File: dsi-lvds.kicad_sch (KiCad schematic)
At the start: 27 parts, among them Q1 PJE138K, U1 TLV70018_SC70, U2 TXB0104_UQFN, U3 SN65DSI84

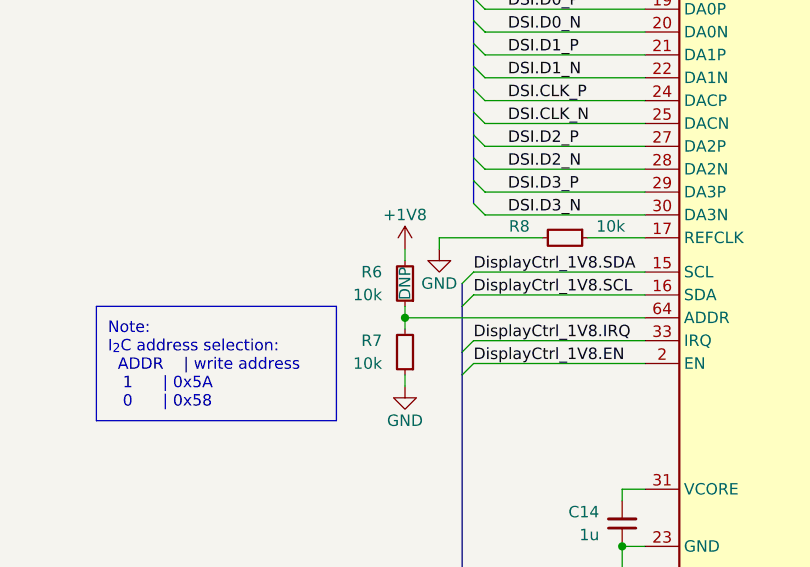
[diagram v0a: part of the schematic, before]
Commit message: [#54932] PCB: move all components inside board outline; Sch: clean DNP's
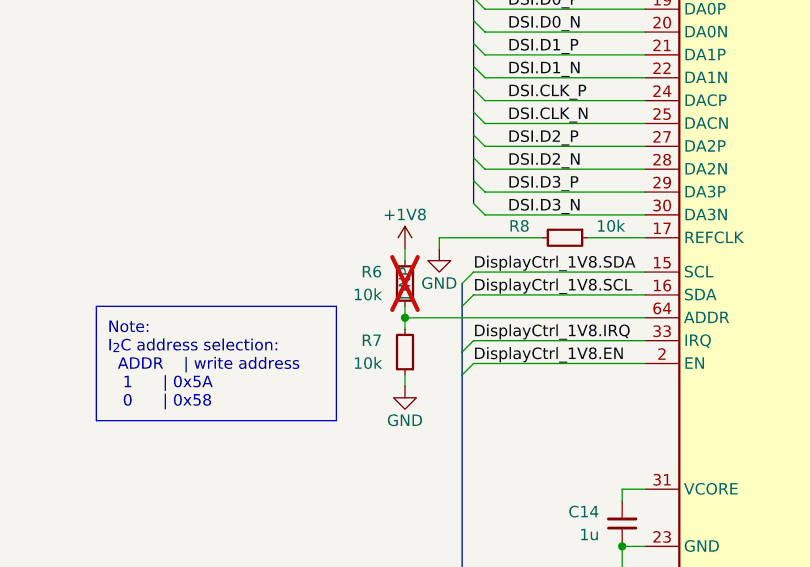
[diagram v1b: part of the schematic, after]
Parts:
- R6: now not fitted; now left out of the parts list
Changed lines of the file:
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@@
   )
   (symbol (lib_id "antmicroResistors0402:R_10k_0402") (at 219.71 135.89 270) (mirror x) (unit 1)
-    (in_bom yes) (on_board yes) (dnp no)
+    (in_bom no) (on_board yes) (dnp yes)
     (property "Reference" "R6" (at 217.17 132.0799 90)
       (effects (font (size 1.27 1.27) (thickness 0.15)) (justify right))

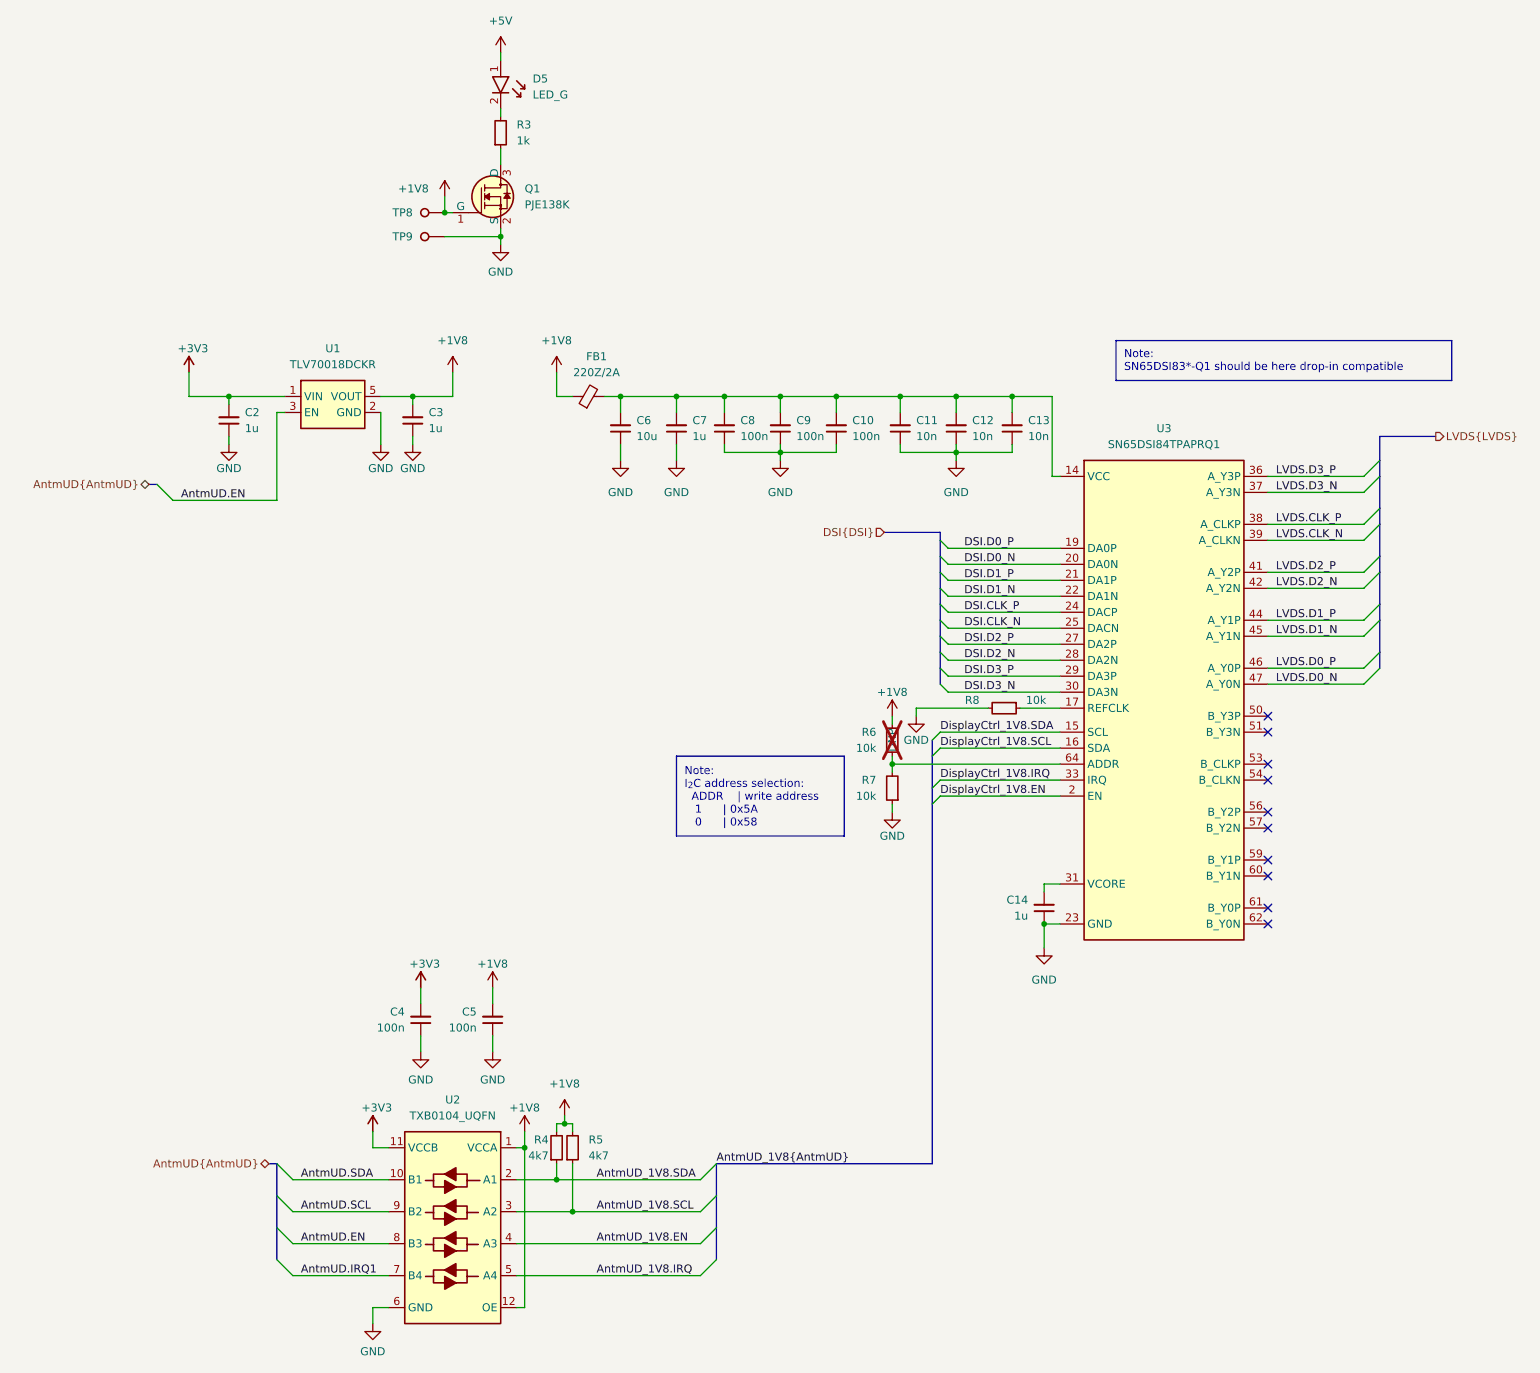
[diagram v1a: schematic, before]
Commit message: [#54932] Sch: update net labels
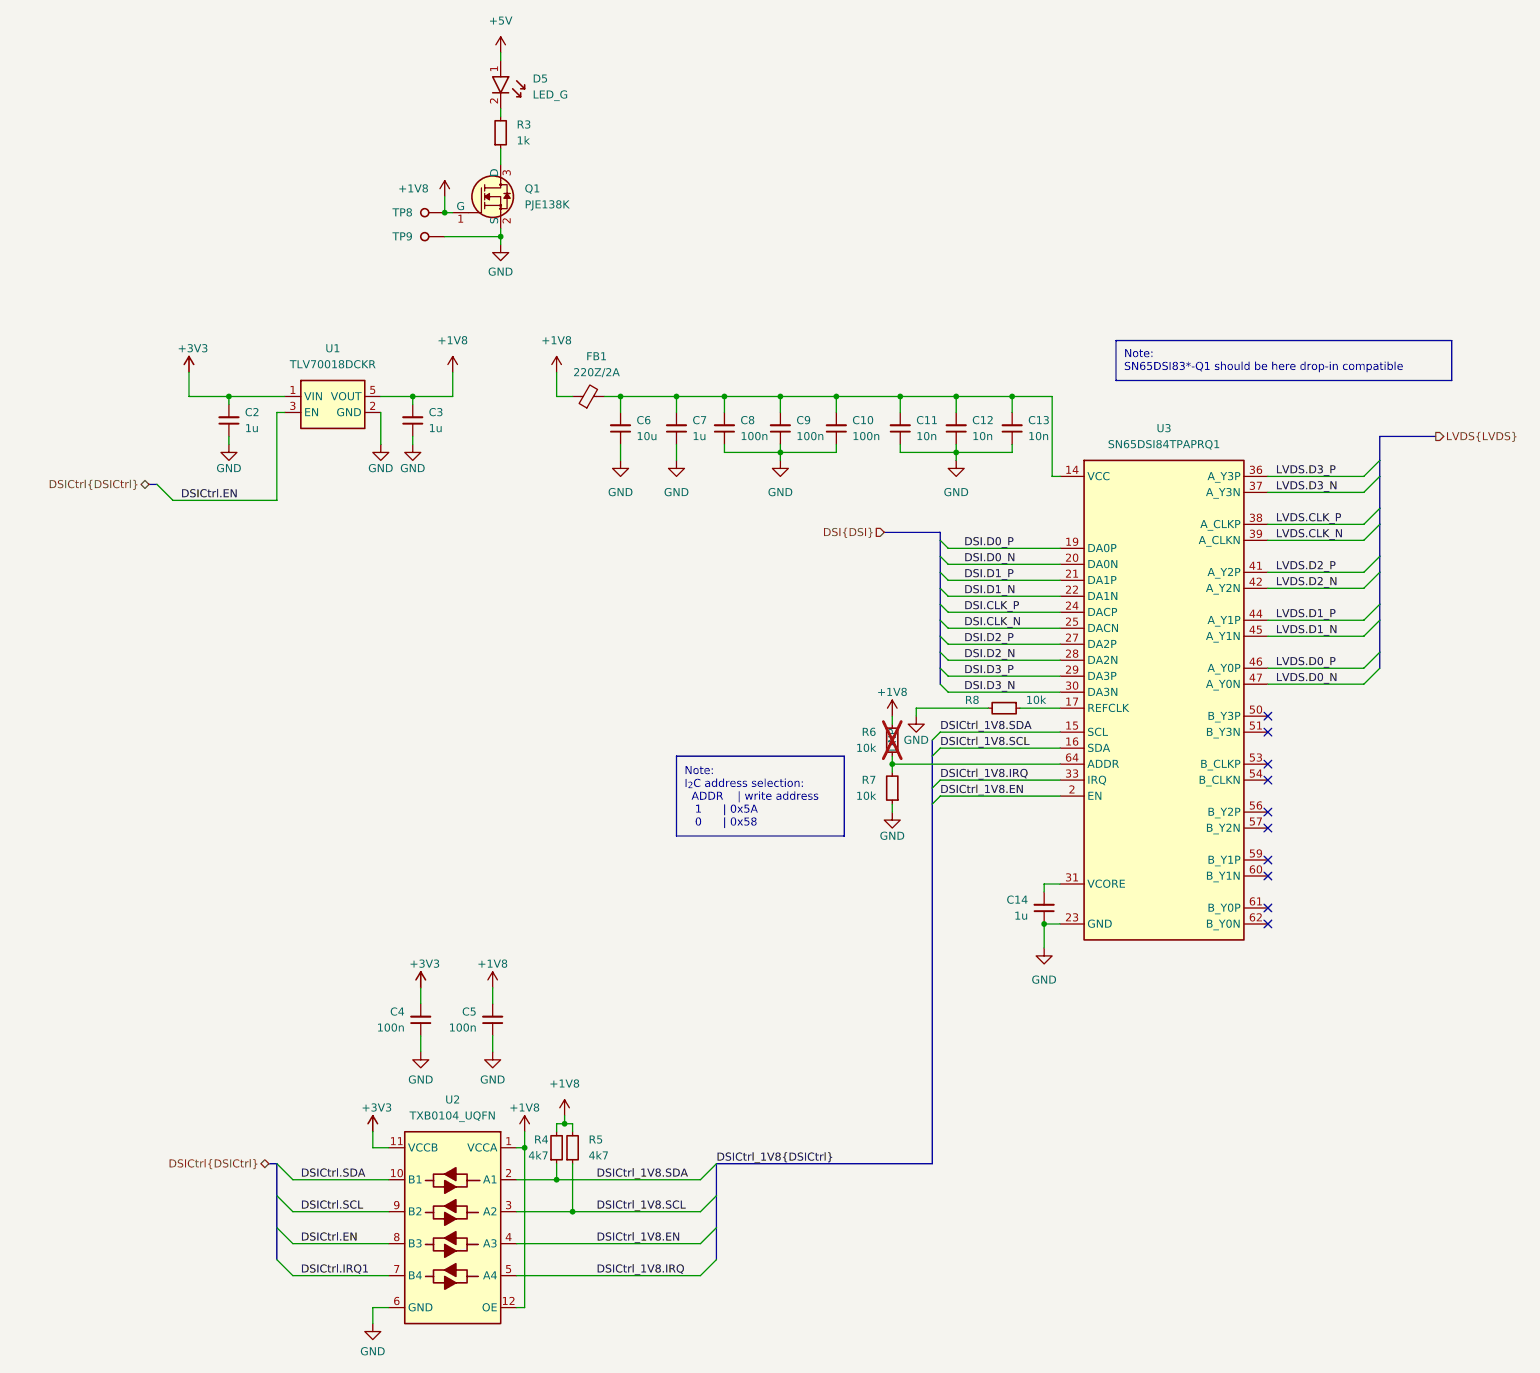
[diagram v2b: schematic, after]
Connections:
- net DisplayCtrl_1V8.EN is gone; now on net DSICtrl_1V8.EN: U3.2 (EN)
- net DisplayCtrl_1V8.IRQ is gone; now on net DSICtrl_1V8.IRQ: U3.33 (IRQ)
- net DisplayCtrl_1V8.SCL is gone; now on net DSICtrl_1V8.SCL: U3.16 (SDA)
- net DisplayCtrl_1V8.SDA is gone; now on net DSICtrl_1V8.SDA: U3.15 (SCL)
- net AntmUD.EN renamed DSICtrl.EN
- net AntmUD.IRQ1 renamed DSICtrl.IRQ1
- net AntmUD.SCL renamed DSICtrl.SCL
- net AntmUD.SDA renamed DSICtrl.SDA
- net AntmUD_1V8.EN renamed DSICtrl_1V8.EN
- net AntmUD_1V8.IRQ renamed DSICtrl_1V8.IRQ
- net AntmUD_1V8.SCL renamed DSICtrl_1V8.SCL
- net AntmUD_1V8.SDA renamed DSICtrl_1V8.SDA
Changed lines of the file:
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@@
     (effects (font (size 1.27 1.27)) (justify left bottom))
   )
-  (label "AntmUD.IRQ1" (at 125.73 218.44 0) (fields_autoplaced)
+  (label "DSICtrl.IRQ1" (at 125.73 218.44 0) (fields_autoplaced)
     (effects (font (size 1.27 1.27)) (justify left bottom))
   )
@@
     (effects (font (size 1.27 1.27)) (justify left bottom))
   )
-  (label "AntmUD.EN" (at 125.73 213.36 0) (fields_autoplaced)
+  (label "DSICtrl.EN" (at 125.73 213.36 0) (fields_autoplaced)
     (effects (font (size 1.27 1.27)) (justify left bottom))
   )
@@
     (effects (font (size 1.27 1.27)) (justify left bottom))
   )
-  (label "DisplayCtrl_1V8.IRQ" (at 227.33 139.7 0) (fields_autoplaced)
+  (label "DSICtrl_1V8.IRQ" (at 227.33 139.7 0) (fields_autoplaced)
     (effects (font (size 1.27 1.27)) (justify left bottom))
   )
@@
     (effects (font (size 1.27 1.27)) (justify left bottom))
   )
-  (label "AntmUD_1V8.SDA" (at 172.72 203.2 0) (fields_autoplaced)
+  (label "DSICtrl_1V8.SDA" (at 172.72 203.2 0) (fields_autoplaced)
     (effects (font (size 1.27 1.27)) (justify left bottom))
   )
-  (label "AntmUD_1V8.IRQ" (at 172.72 218.44 0) (fields_autoplaced)
+  (label "DSICtrl_1V8.IRQ" (at 172.72 218.44 0) (fields_autoplaced)
     (effects (font (size 1.27 1.27)) (justify left bottom))
   )
@@
     (effects (font (size 1.27 1.27)) (justify left bottom))
   )
-  (label "AntmUD.EN" (at 106.68 95.25 0) (fields_autoplaced)
+  (label "DSICtrl.EN" (at 106.68 95.25 0) (fields_autoplaced)
     (effects (font (size 1.27 1.27)) (justify left bottom))
   )
@@
     (effects (font (size 1.27 1.27)) (justify left bottom))
   )
-  (label "AntmUD.SCL" (at 125.73 208.28 0) (fields_autoplaced)
+  (label "DSICtrl.SCL" (at 125.73 208.28 0) (fields_autoplaced)
     (effects (font (size 1.27 1.27)) (justify left bottom))
   )
@@
     (effects (font (size 1.27 1.27)) (justify left bottom))
   )
-  (label "DisplayCtrl_1V8.SDA" (at 227.33 132.08 0) (fields_autoplaced)
+  (label "DSICtrl_1V8.SDA" (at 227.33 132.08 0) (fields_autoplaced)
     (effects (font (size 1.27 1.27)) (justify left bottom))
   )
@@
     (effects (font (size 1.27 1.27)) (justify left bottom))
   )
-  (label "AntmUD_1V8.EN" (at 172.72 213.36 0) (fields_autoplaced)
+  (label "DSICtrl_1V8.EN" (at 172.72 213.36 0) (fields_autoplaced)
     (effects (font (size 1.27 1.27)) (justify left bottom))
   )
@@
     (effects (font (size 1.27 1.27)) (justify left bottom))
   )
-  (label "AntmUD_1V8.SCL" (at 172.72 208.28 0) (fields_autoplaced)
+  (label "DSICtrl_1V8.SCL" (at 172.72 208.28 0) (fields_autoplaced)
     (effects (font (size 1.27 1.27)) (justify left bottom))
   )
-  (label "DisplayCtrl_1V8.SCL" (at 227.33 134.62 0) (fields_autoplaced)
+  (label "DSICtrl_1V8.SCL" (at 227.33 134.62 0) (fields_autoplaced)
     (effects (font (size 1.27 1.27)) (justify left bottom))
   )
-  (label "AntmUD_1V8{AntmUD}" (at 191.77 200.66 0) (fields_autoplaced)
+  (label "DSICtrl_1V8{DSICtrl}" (at 191.77 200.66 0) (fields_autoplaced)
     (effects (font (size 1.27 1.27)) (justify left bottom))
   )
@@
     (effects (font (size 1.27 1.27)) (justify left bottom))
   )
-  (label "AntmUD.SDA" (at 125.73 203.2 0) (fields_autoplaced)
+  (label "DSICtrl.SDA" (at 125.73 203.2 0) (fields_autoplaced)
     (effects (font (size 1.27 1.27)) (justify left bottom))
   )
-  (label "DisplayCtrl_1V8.EN" (at 227.33 142.24 0) (fields_autoplaced)
+  (label "DSICtrl_1V8.EN" (at 227.33 142.24 0) (fields_autoplaced)
     (effects (font (size 1.27 1.27)) (justify left bottom))
   )
@@
     (effects (font (size 1.27 1.27)) (justify left bottom))
   )
-  (hierarchical_label "AntmUD{AntmUD}" (shape bidirectional) (at 101.6 92.71 180) (fields_autoplaced)
+  (hierarchical_label "DSICtrl{DSICtrl}" (shape bidirectional) (at 101.6 92.71 180) (fields_autoplaced)
     (effects (font (size 1.27 1.27)) (justify right))
   )
-  (hierarchical_label "AntmUD{AntmUD}" (shape bidirectional) (at 120.65 200.66 180) (fields_autoplaced)
+  (hierarchical_label "DSICtrl{DSICtrl}" (shape bidirectional) (at 120.65 200.66 180) (fields_autoplaced)
     (effects (font (size 1.27 1.27)) (justify right))
   )

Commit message: [#54932] Add changes requested in review
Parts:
- removed C10, C4, C5, C8, C9: C_100n_0402, antmicro-footprints:C_0402_1005Metric, symbol antmicroCapacitors0402:C_100n_0402
- removed C11, C12, C13: C_10n_0402, antmicro-footprints:C_0402_1005Metric, symbol antmicroCapacitors0402:C_10n_0402
- removed C14, C2, C3, C7: C_1u_0402, antmicro-footprints:C_0402_1005Metric, symbol antmicroCapacitors0402:C_1u_0402
- removed C6: C_10u_0402, antmicro-footprints:C_0402_1005Metric, symbol antmicroCapacitors0402:C_10u_0402
- removed D5: LED_G, antmicro-footprints:LED_0603_1608Metric_R, symbol antmicroLEDIndicationDiscrete:LED_R_0603_598-8D80-107F
- removed FB1: 220Z/2A, antmicro-footprints:FB_0603_1608Metric, symbol antmicroFerriteBeadsandChips:FB_220Z_2.2A_TDK-MPZ_0603
- removed Q1: PJE138K, antmicro-footprints:SOT-523, symbol antmicroTransistorsFETsMOSFETsSingle:PJE138K
- removed R3: R_1k_0402, antmicro-footprints:R_0402_1005Metric, symbol antmicroResistors0402:R_1k_0402
- removed R4, R5: R_4k7_0402, antmicro-footprints:R_0402_1005Metric, symbol antmicroResistors0402:R_4k7_0402
- removed R6, R7, R8: R_10k_0402, antmicro-footprints:R_0402_1005Metric, symbol antmicroResistors0402:R_10k_0402
- removed TP8, TP9: TP_1mm_SMD, antmicro-footprints:TP_SMD_1mm, symbol antmicroTestPoints:TP_1mm_SMD
- removed U1: TLV70018_SC70, antmicro-footprints:SC-70-5, symbol antmicroPMICVoltageRegulatorsLinear:TLV70018_SC70
- removed U2: TXB0104_UQFN, antmicro-footprints:UQFN-12_2x1.7mm_P0.4mm_Texas_RUT, symbol antmicroLogicTranslatorsLevelShifters:TXB0104_UQFN
- removed U3: SN65DSI84, antmicro-footprints:HTQFP-64_10x10mm_P0.5mm, symbol antmicroInterfaceControllers:SN65DSI84
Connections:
- no-connect marks 10 -> 0
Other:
- note removed: "Note: I_{2}C address selection: ADDR | write address 1 | 0x5A 0 | 0x58"
- note removed: "Note: SN65DSI83*-Q1 should be here drop-in compatible"
